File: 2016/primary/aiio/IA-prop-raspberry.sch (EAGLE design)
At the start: 108 parts, among them U1 ARDUINO_R3_SHIELD

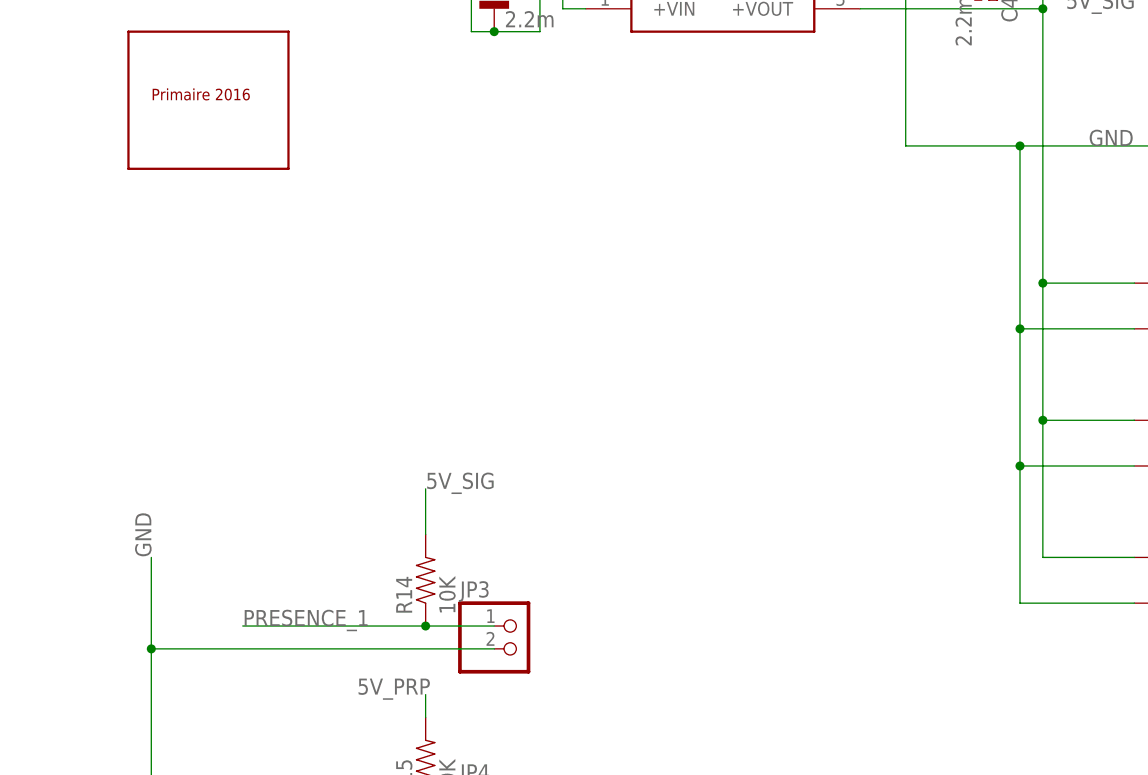
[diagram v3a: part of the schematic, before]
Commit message: [AIIO_board] Add 3v3 reglator and connectors on .sch and .board files.
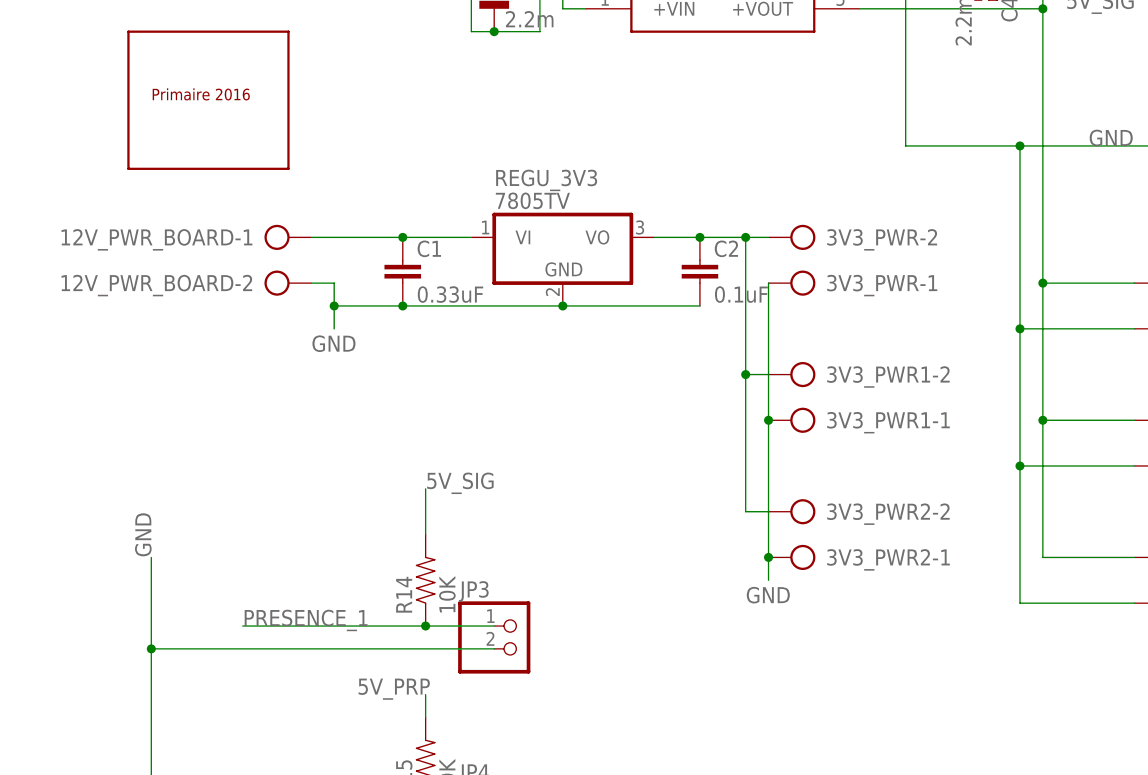
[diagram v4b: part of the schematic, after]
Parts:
- added 12V_PWR_BOARD, 3V3_PWR, 3V3_PWR1, 3V3_PWR2: (no value), con-ptr500:AK300/2
- added C1: 0.33uF, rcl:C-EU050-025X075
- added C2: 0.1uF, rcl:C-EU050-025X075
- added REGU_3V3: 7805TV, linear:7805TV
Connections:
- new net N$71: 12V_PWR_BOARD-1.KL, C1.1, REGU_3V3.VI
- new net N$72: 3V3_PWR-2.KL, 3V3_PWR1-2.KL, 3V3_PWR2-2.KL, C2.1, REGU_3V3.VO
- net GND: now also 12V_PWR_BOARD-2.KL, 3V3_PWR-1.KL, 3V3_PWR1-1.KL, 3V3_PWR2-1.KL, C1.2, C2.2, REGU_3V3.GND
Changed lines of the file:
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@@
 <part name="JP9" library="pinhead" deviceset="PINHD-1X3" device=""/>
 <part name="CON_I2C_SONARS" library="pinhead" deviceset="PINHD-1X4" device=""/>
+<part name="REGU_3V3" library="linear" deviceset="78*" device="TV" technology="05"/>
+<part name="12V_PWR_BOARD" library="con-ptr500" deviceset="AK300/2" device="">
+<attribute name="MF" value=""/>
+<attribute name="MPN" value=""/>
+<attribute name="OC_FARNELL" value="unknown"/>
+<attribute name="OC_NEWARK" value="unknown"/>
+</part>
+<part name="C1" library="rcl" deviceset="C-EU" device="050-025X075" value="0.33uF"/>
+<part name="C2" library="rcl" deviceset="C-EU" device="050-025X075" value="0.1uF"/>
+<part name="3V3_PWR" library="con-ptr500" deviceset="AK300/2" device="">
+<attribute name="MF" value=""/>
+<attribute name="MPN" value=""/>
+<attribute name="OC_FARNELL" value="unknown"/>
+<attribute name="OC_NEWARK" value="unknown"/>
+</part>
+<part name="3V3_PWR1" library="con-ptr500" deviceset="AK300/2" device="">
+<attribute name="MF" value=""/>
+<attribute name="MPN" value=""/>
+<attribute name="OC_FARNELL" value="unknown"/>
+<attribute name="OC_NEWARK" value="unknown"/>
+</part>
+<part name="3V3_PWR2" library="con-ptr500" deviceset="AK300/2" device="">
+<attribute name="MF" value=""/>
+<attribute name="MPN" value=""/>
+<attribute name="OC_FARNELL" value="unknown"/>
+<attribute name="OC_NEWARK" value="unknown"/>
+</part>
 </parts>
 <sheets>
@@
 <instance part="JP9" gate="A" x="193.04" y="-121.92" rot="R270"/>
 <instance part="CON_I2C_SONARS" gate="A" x="259.08" y="-43.18" rot="R180"/>
+<instance part="REGU_3V3" gate="A1" x="-25.4" y="0"/>
+<instance part="12V_PWR_BOARD" gate="-1" x="-58.42" y="0"/>
+<instance part="12V_PWR_BOARD" gate="-2" x="-58.42" y="-5.08"/>
+<instance part="C1" gate="G$1" x="-43.18" y="-2.54"/>
+<instance part="C2" gate="G$1" x="-10.16" y="-2.54"/>
+<instance part="3V3_PWR" gate="-1" x="2.54" y="-5.08" rot="R180"/>
+<instance part="3V3_PWR" gate="-2" x="2.54" y="0" rot="R180"/>
+<instance part="3V3_PWR1" gate="-1" x="2.54" y="-20.32" rot="R180"/>
+<instance part="3V3_PWR1" gate="-2" x="2.54" y="-15.24" rot="R180"/>
+<instance part="3V3_PWR2" gate="-1" x="2.54" y="-35.56" rot="R180"/>
+<instance part="3V3_PWR2" gate="-2" x="2.54" y="-30.48" rot="R180"/>
 </instances>
 <busses>
@@
 <wire x1="198.12" y1="-127" x2="215.9" y2="-127" width="0.1524" layer="91"/>
 </segment>
+<segment>
+<pinref part="12V_PWR_BOARD" gate="-2" pin="KL"/>
+<wire x1="-53.34" y1="-5.08" x2="-50.8" y2="-5.08" width="0.1524" layer="91"/>
+<wire x1="-50.8" y1="-5.08" x2="-50.8" y2="-7.62" width="0.1524" layer="91"/>
+<label x="-53.34" y="-12.7" size="1.778" layer="95"/>
+<pinref part="C1" gate="G$1" pin="2"/>
+<wire x1="-50.8" y1="-7.62" x2="-50.8" y2="-10.16" width="0.1524" layer="91"/>
+<wire x1="-50.8" y1="-7.62" x2="-43.18" y2="-7.62" width="0.1524" layer="91"/>
+<junction x="-50.8" y="-7.62"/>
+<pinref part="REGU_3V3" gate="A1" pin="GND"/>
+<wire x1="-43.18" y1="-7.62" x2="-25.4" y2="-7.62" width="0.1524" layer="91"/>
+<junction x="-43.18" y="-7.62"/>
+<pinref part="C2" gate="G$1" pin="2"/>
+<wire x1="-25.4" y1="-7.62" x2="-10.16" y2="-7.62" width="0.1524" layer="91"/>
+<junction x="-25.4" y="-7.62"/>
+</segment>
+<segment>
+<pinref part="3V3_PWR" gate="-1" pin="KL"/>
+<pinref part="3V3_PWR1" gate="-1" pin="KL"/>
+<wire x1="-2.54" y1="-5.08" x2="-2.54" y2="-20.32" width="0.1524" layer="91"/>
+<pinref part="3V3_PWR2" gate="-1" pin="KL"/>
+<wire x1="-2.54" y1="-35.56" x2="-2.54" y2="-20.32" width="0.1524" layer="91"/>
+<junction x="-2.54" y="-20.32"/>
+<wire x1="-2.54" y1="-35.56" x2="-2.54" y2="-38.1" width="0.1524" layer="91"/>
+<junction x="-2.54" y="-35.56"/>
+<label x="-5.08" y="-40.64" size="1.778" layer="95"/>
+</segment>
 </net>
 <net name="N$4" class="0">
@@
 </segment>
 </net>
+<net name="N$71" class="0">
+<segment>
+<pinref part="12V_PWR_BOARD" gate="-1" pin="KL"/>
+<pinref part="C1" gate="G$1" pin="1"/>
+<wire x1="-53.34" y1="0" x2="-43.18" y2="0" width="0.1524" layer="91"/>
+<pinref part="REGU_3V3" gate="A1" pin="VI"/>
+<wire x1="-43.18" y1="0" x2="-35.56" y2="0" width="0.1524" layer="91"/>
+<junction x="-43.18" y="0"/>
+</segment>
+</net>
+<net name="N$72" class="0">
+<segment>
+<pinref part="REGU_3V3" gate="A1" pin="VO"/>
+<pinref part="C2" gate="G$1" pin="1"/>
+<wire x1="-15.24" y1="0" x2="-10.16" y2="0" width="0.1524" layer="91"/>
+<wire x1="-10.16" y1="0" x2="-5.08" y2="0" width="0.1524" layer="91"/>
+<junction x="-10.16" y="0"/>
+<pinref part="3V3_PWR" gate="-2" pin="KL"/>
+<wire x1="-5.08" y1="0" x2="-2.54" y2="0" width="0.1524" layer="91"/>
+<wire x1="-5.08" y1="0" x2="-5.08" y2="-15.24" width="0.1524" layer="91"/>
+<junction x="-5.08" y="0"/>
+<pinref part="3V3_PWR1" gate="-2" pin="KL"/>
+<wire x1="-5.08" y1="-15.24" x2="-2.54" y2="-15.24" width="0.1524" layer="91"/>
+<wire x1="-5.08" y1="-15.24" x2="-5.08" y2="-30.48" width="0.1524" layer="91"/>
+<junction x="-5.08" y="-15.24"/>
+<pinref part="3V3_PWR2" gate="-2" pin="KL"/>
+<wire x1="-5.08" y1="-30.48" x2="-2.54" y2="-30.48" width="0.1524" layer="91"/>
+</segment>
+</net>

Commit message: [AIIO_board] Add button and connector for IHM. Remove useless pull-up resistors.
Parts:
- removed R11, R12, R13, R14, R15, R16, R17, R18: 10K, SparkFun:RESISTORAXIAL-0.3
- added U$12: PUSH_BUT_COL_SELEC, club:PUSH_BUT_COL_SELEC
- BOARDIHM_CON_IHM: device con-lsta:FE06-1 -> con-lsta:FE07-1
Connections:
- removed net 5VSIG: R13.2
- removed net 5V_PRP: R15.2, R16.2, R17.2, R18.2
- new net N$73: BOARDIHM_CON_IHM.7, U$12.P$1
- net 5V_SIG: no longer R11.2, R12.2, R14.2
- net BOARDIHM_GND: now also U$12.P$2
- net N$46: no longer R11.1
- net N$47: no longer R12.1
- net N$49: no longer R13.1
- net PRESENCE_1: no longer R14.1
- net PRESENCE_2: no longer R15.1
- net PRESENCE_3: no longer R16.1
- net PRESENCE_4: no longer R17.1
- net PRESENCE_5: no longer R18.1
